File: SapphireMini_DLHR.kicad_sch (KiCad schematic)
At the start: 14 parts, among them IC201 DLHR-F50D-E1BD-C-NAV8, U201 LIS2DH12TR, U202 BMP390

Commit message: Partial Routing
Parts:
- removed R201: EXB-2HV470JV, Sapphire:EXB-2HV470JV, symbol sapphireMini:EXB-2HV470JV_1
- added R201, R204, R205, R208, R209, R210: 47, Resistor_SMD:R_0603_1608Metric, symbol Device:R_US
- C201: value 22uF -> 1uF; Attrition 0 -> (none); DPN 1276-2728-1-ND -> 1276-6471-1-ND; Digi-Key_PN 445-12847-1-ND -> 1276-6471-1-ND; DigiKey Price 0.42 -> 0.06; MPN CL21A226MAYNNNE -> CL21B105KOFNNNG; MacroFab_PN CC1206ZKY5V7BB226 -> MF-CAP-0805-1uF; Tolerance 20% -> 10%; Type (none) -> (none); Voltage Rating (DC) 16 volt -> (none); Working Voltage(DC) 6.3volts -> (none)
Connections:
- net I2C_SCL: now also R201.2, R205.2, R209.2
- net I2C_SDA: now also R204.2, R208.2, R210.2
- net at U201.4 (SDA/SDI/SDO): now also R208.1
- net at U201.1 (SCL/SPC): now also R205.1
- net BMP_SCK: no longer names the net of U202.2 (SCK)
- net BMP_SCK: now also R209.1
- net BMP_SDI: no longer names the net of U202.4 (SDI)
- net BMP_SDI: now also R210.1
- net DLHR_SCL: no longer names the net of IC201.4 (SCL/SCLK)
- net DLHR_SCL: now also R201.1
- net DLHR_SDA: no longer names the net of IC201.3 (SDA/MOSI)
- net DLHR_SDA: now also R204.1
- no-connect marks 4 -> 2

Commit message: Added slot for wiring
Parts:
- R201, R204, R205, R208, R209, R210: Manufacturer (none) -> Vishay
- R206: MPN CRCW060347R0FKEAC -> CRCW060310K0FKEAC
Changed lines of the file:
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@@
       (effects (font (size 1.27 1.27)) hide)
     )
-    (property "MPN" "CRCW060347R0FKEAC" (id 5) (at 115.57 133.35 0)
+    (property "MPN" "CRCW060310K0FKEAC" (id 5) (at 115.57 133.35 0)
       (effects (font (size 1.27 1.27)) hide)
     )
@@
       (effects (font (size 1.27 1.27)) hide)
     )
-    (property "Description" "47 Ohms ±1% 0.1W, 1/10W Chip Resistor 0603" (id 13) (at 115.57 133.35 0)
+    (property "Description" "10K Ohms ±1% 0.1W, 1/10W Chip Resistor 0603" (id 13) (at 115.57 133.35 0)
       (effects (font (size 1.27 1.27)) hide)
     )
@@
       (effects (font (size 1.27 1.27)) hide)
     )
+    (property "Manufacturer" "Vishay" (id 6) (at 76.2 152.4 0)
+      (effects (font (size 1.27 1.27)) hide)
+    )
     (pin "1")
     (pin "2")
@@
       (effects (font (size 1.27 1.27)) hide)
     )
+    (property "Manufacturer" "Vishay" (id 6) (at 76.2 147.32 0)
+      (effects (font (size 1.27 1.27)) hide)
+    )
     (pin "1")
     (pin "2")
@@
     )
     (property "MPN" "CRCW060347R0FKEAC" (id 5) (at 60.96 76.2 0)
+      (effects (font (size 1.27 1.27)) hide)
+    )
+    (property "Manufacturer" "Vishay" (id 6) (at 60.96 76.2 0)
       (effects (font (size 1.27 1.27)) hide)
     )
@@
       (effects (font (size 1.27 1.27)) hide)
     )
+    (property "Manufacturer" "Vishay" (id 6) (at 182.88 39.37 0)
+      (effects (font (size 1.27 1.27)) hide)
+    )
     (pin "1")
     (pin "2")
@@
       (effects (font (size 1.27 1.27)) hide)
     )
+    (property "Manufacturer" "Vishay" (id 6) (at 62.23 64.77 0)
+      (effects (font (size 1.27 1.27)) hide)
+    )
     (pin "1")
     (pin "2")
@@
       (effects (font (size 1.27 1.27)) hide)
     )
+    (property "Manufacturer" "Vishay" (id 6) (at 182.88 44.45 0)
+      (effects (font (size 1.27 1.27)) hide)
+    )

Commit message: OSH_ParkM2R3
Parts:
- FB201, R201, R204, R205, R208, R209, R210: Populate (none) -> 1
- IC201: value DLHR-F50D-E1BD-C-NAV8 -> DNP DLHR-F50D-E1BD-C-NAV8
- U201: value LIS2DH12TR -> LIS2HH12TR; Populate (none) -> 1
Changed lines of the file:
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@@
     (in_bom yes) (on_board yes)
     (property "Reference" "IC201" (id 0) (at 90.17 25.019 0))
-    (property "Value" "DLHR-F50D-E1BD-C-NAV8" (id 1) (at 90.17 27.3304 0))
+    (property "Value" "DNP DLHR-F50D-E1BD-C-NAV8" (id 1) (at 90.17 27.3304 0))
     (property "Footprint" "Sapphire:DLHRF50DE1BDCNAV8" (id 2) (at 102.87 29.21 0)
       (effects (font (size 1.27 1.27)) (justify left) hide)
@@
     )
     (property "Status" "" (id 19) (at 73.66 31.75 0)
+      (effects (font (size 1.27 1.27)) hide)
+    )
+    (property "Consign" "" (id 20) (at 73.66 31.75 0)
       (effects (font (size 1.27 1.27)) hide)
     )
@@
       (effects (font (size 1.524 1.524)))
     )
-    (property "Value" "LIS2DH12TR" (id 1) (at 166.2657 145.3656 0)
+    (property "Value" "LIS2HH12TR" (id 1) (at 166.2657 145.3656 0)
       (effects (font (size 1.524 1.524)))
     )
@@
     (property "Status" "Active" (id 12) (at 156.21 115.57 0)
       (effects (font (size 1.524 1.524)) (justify left) hide)
+    )
+    (property "Populate" "1" (id 13) (at 151.13 146.05 0)
+      (effects (font (size 1.27 1.27)) hide)
     )
     (pin "1")
@@
       (effects (font (size 1.27 1.27)) hide)
     )
+    (property "Populate" "1" (id 7) (at 76.2 152.4 0)
+      (effects (font (size 1.27 1.27)) hide)
+    )
     (pin "1")
     (pin "2")
@@
       (effects (font (size 1.27 1.27)) hide)
     )
+    (property "Populate" "1" (id 7) (at 76.2 147.32 0)
+      (effects (font (size 1.27 1.27)) hide)
+    )
     (pin "1")
     (pin "2")
@@
     )
     (property "Manufacturer" "Vishay" (id 6) (at 60.96 76.2 0)
+      (effects (font (size 1.27 1.27)) hide)
+    )
+    (property "Populate" "1" (id 7) (at 60.96 76.2 0)
       (effects (font (size 1.27 1.27)) hide)
     )
@@
       (effects (font (size 1.27 1.27)) hide)
     )
+    (property "Populate" "1" (id 6) (at 46.99 34.29 0)
+      (effects (font (size 1.27 1.27)) hide)
+    )
     (pin "1")
     (pin "2")
@@
       (effects (font (size 1.27 1.27)) hide)
     )
+    (property "Populate" "1" (id 7) (at 182.88 39.37 0)
+      (effects (font (size 1.27 1.27)) hide)
+    )
     (pin "1")
     (pin "2")
@@
       (effects (font (size 1.27 1.27)) hide)
     )
+    (property "Populate" "1" (id 7) (at 62.23 64.77 0)
+      (effects (font (size 1.27 1.27)) hide)
+    )
     (pin "1")
     (pin "2")
@@
       (effects (font (size 1.27 1.27)) hide)
     )
+    (property "Populate" "1" (id 7) (at 182.88 44.45 0)
+      (effects (font (size 1.27 1.27)) hide)
+    )

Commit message: Board ready for final check
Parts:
- added AC201: IIM-42351, IIM42352, symbol sapphireMini:IIM-42351
- added C204, C206: 100nF, Capacitor_SMD:C_0402_1005Metric, symbol Device:C_Small
- added R211, R212, R213, R214: 47, Resistor_SMD:R_0603_1608Metric, symbol Device:R_US
- added R215: DNP 47, Resistor_SMD:R_0603_1608Metric, symbol Device:R_US
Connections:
- net GND: now also AC201.6 (GND), AC201.7 (RESV_3), C204.2, C206.2
- net I2C_SCL: now also R212.2
- net I2C_SDA: now also R211.2
- net P3V3: now also AC201.1 (AP_SDO_/_AP_AD0), AC201.12 (AP_CS), AC201.5 (VDDIO), AC201.8 (VDD), C204.1, C206.1
- net WIFI_IRQ: now also R214.1
- new net: AC201.9 (INT2_/_FSYNC), R213.2, R215.2
- new net: AC201.14 (AP_SDA_/_AP_SDIO_/_AP_SDI), R212.1
- new net: AC201.13 (AP_SCL_/_AP_SCLK), R211.1
- new net: AC201.4 (INT1_/_INT), R214.2
- new net 32KHz: R215.1
- new net SPARE: R213.1
- no-connect marks 2 -> 6
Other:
- note added: "DS3231 address 0x68"
- note added: "IM-42351 address 0x69"
- note added: "IM42351 Low Noise Accelerometer"
- moved on the sheet: C205, R202, R203, R205, R206, R208, U201

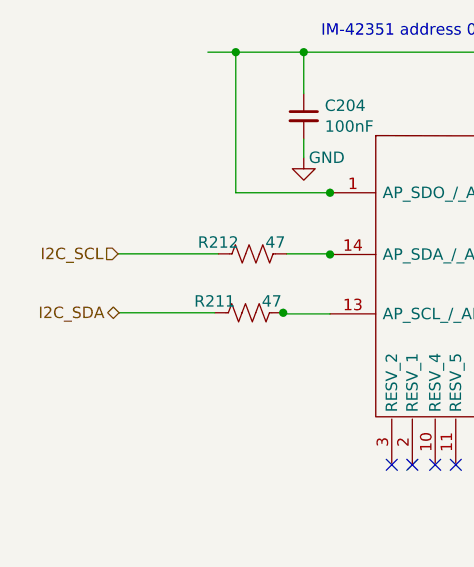
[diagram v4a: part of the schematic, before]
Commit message: Updated to correct wiring of IIM42351
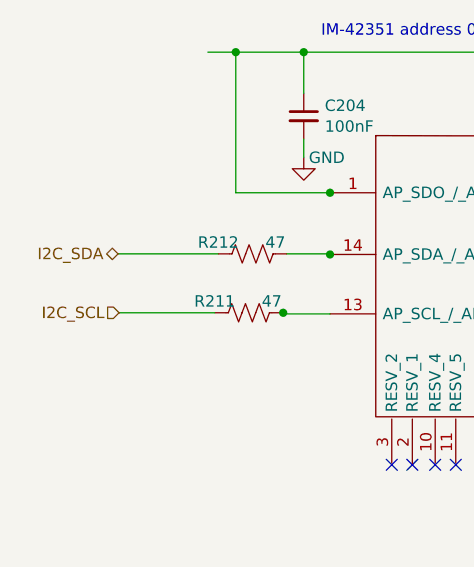
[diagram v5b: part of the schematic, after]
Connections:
- net I2C_SCL: now also R211.2; no longer R212.2
- net I2C_SDA: now also R212.2; no longer R211.2
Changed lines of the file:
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@@
     (effects (font (size 1.27 1.27)) (justify left))
   )
-  (hierarchical_label "I2C_SDA" (shape bidirectional) (at 27.7403 144.78 180)
+  (hierarchical_label "I2C_SDA" (shape bidirectional) (at 27.6253 138.236 180)
     (effects (font (size 1.27 1.27)) (justify right))
   )
@@
     (effects (font (size 1.27 1.27)) (justify left))
   )
-  (hierarchical_label "I2C_SCL" (shape input) (at 27.6253 138.236 180)
+  (hierarchical_label "I2C_SCL" (shape input) (at 27.7403 144.78 180)
     (effects (font (size 1.27 1.27)) (justify right))
   )

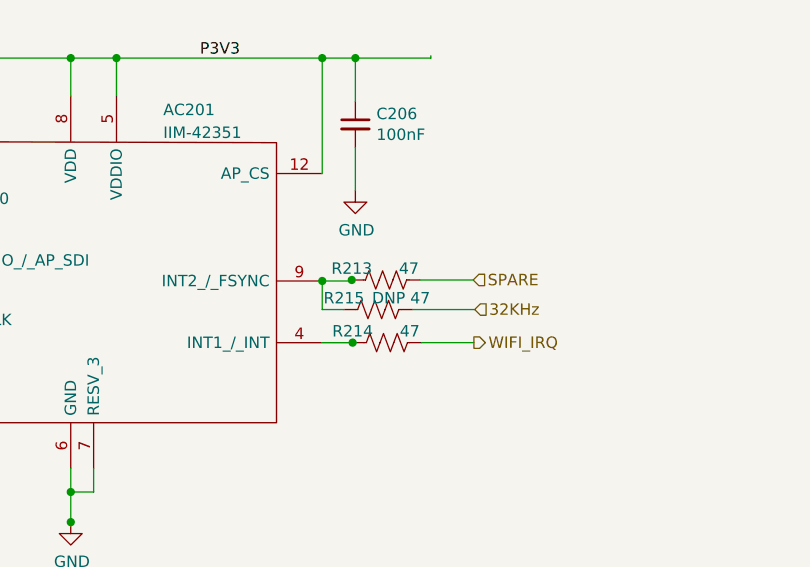
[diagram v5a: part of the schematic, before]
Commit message: Updated for 32KHz input on IIM42351
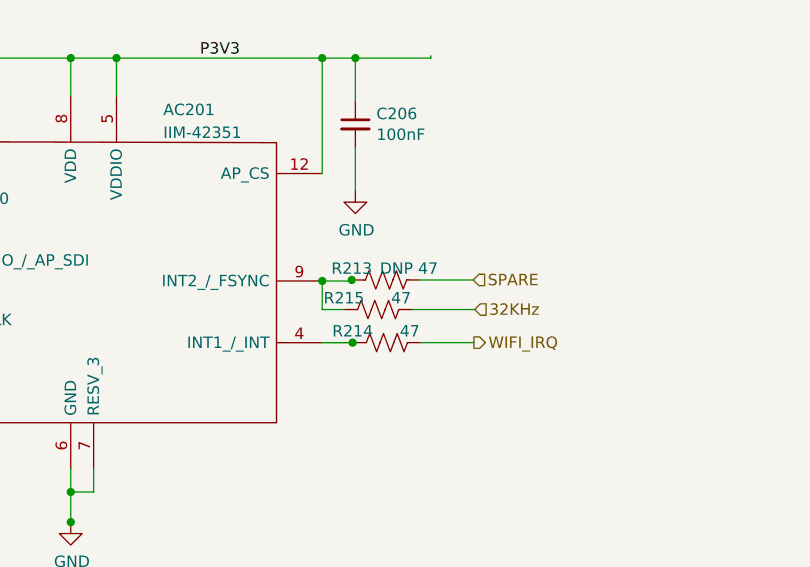
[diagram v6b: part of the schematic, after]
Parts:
- R213: value 47 -> DNP 47; Populate 1 -> 0; now left out of the parts list
- R215: value DNP 47 -> 47; Populate 0 -> 1; now in the parts list
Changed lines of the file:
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@@
   )
   (symbol (lib_id "Device:R_US") (at 114.9138 140.4775 270) (unit 1)
-    (in_bom yes) (on_board yes)
+    (in_bom no) (on_board yes)
     (property "Reference" "R213" (id 0) (at 111.1038 139.2075 90))
-    (property "Value" "47" (id 1) (at 117.4538 139.2075 90))
+    (property "Value" "DNP 47" (id 1) (at 117.4538 139.2075 90))
     (property "Footprint" "Resistor_SMD:R_0603_1608Metric" (id 2) (at 114.6598 141.4935 90)
       (effects (font (size 1.27 1.27)) hide)
@@
       (effects (font (size 1.27 1.27)) hide)
     )
-    (property "Populate" "1" (id 7) (at 114.9138 140.4775 0)
+    (property "Populate" "0" (id 7) (at 114.9138 140.4775 0)
       (effects (font (size 1.27 1.27)) hide)
     )
@@
   )
   (symbol (lib_id "Device:R_US") (at 114.046 143.764 270) (unit 1)
-    (in_bom no) (on_board yes)
+    (in_bom yes) (on_board yes)
     (property "Reference" "R215" (id 0) (at 110.236 142.494 90))
-    (property "Value" "DNP 47" (id 1) (at 116.586 142.494 90))
+    (property "Value" "47" (id 1) (at 116.586 142.494 90))
     (property "Footprint" "Resistor_SMD:R_0603_1608Metric" (id 2) (at 113.792 144.78 90)
       (effects (font (size 1.27 1.27)) hide)
@@
       (effects (font (size 1.27 1.27)) hide)
     )
-    (property "Populate" "0" (id 7) (at 114.046 143.764 0)
-      (effects (font (size 1.27 1.27)) hide)
-    )
+    (property "Populate" "1" (id 7) (at 114.046 143.764 0)
+      (effects (font (size 1.27 1.27)) hide)
+    )
